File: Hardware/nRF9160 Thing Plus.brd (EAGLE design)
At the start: 58.4 x 22.9 mm, 128 parts, among them J1 USB Female C, J10 QWIIC_RIGHT_ANGLE, J2 CON-HEADER-1X12-MALE-PIN, J3 CON-HEADER-1X16-MALE-PIN, J4 CON-1909763-1, J6 CON-SIM-104224-0820, J7 CON-1909763-1, J8 CON-FTSH-105-XX-X-DV, Q1 MOSFET-P-SC89, Q2 MOSFET-DUAL-COMP-SOT563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

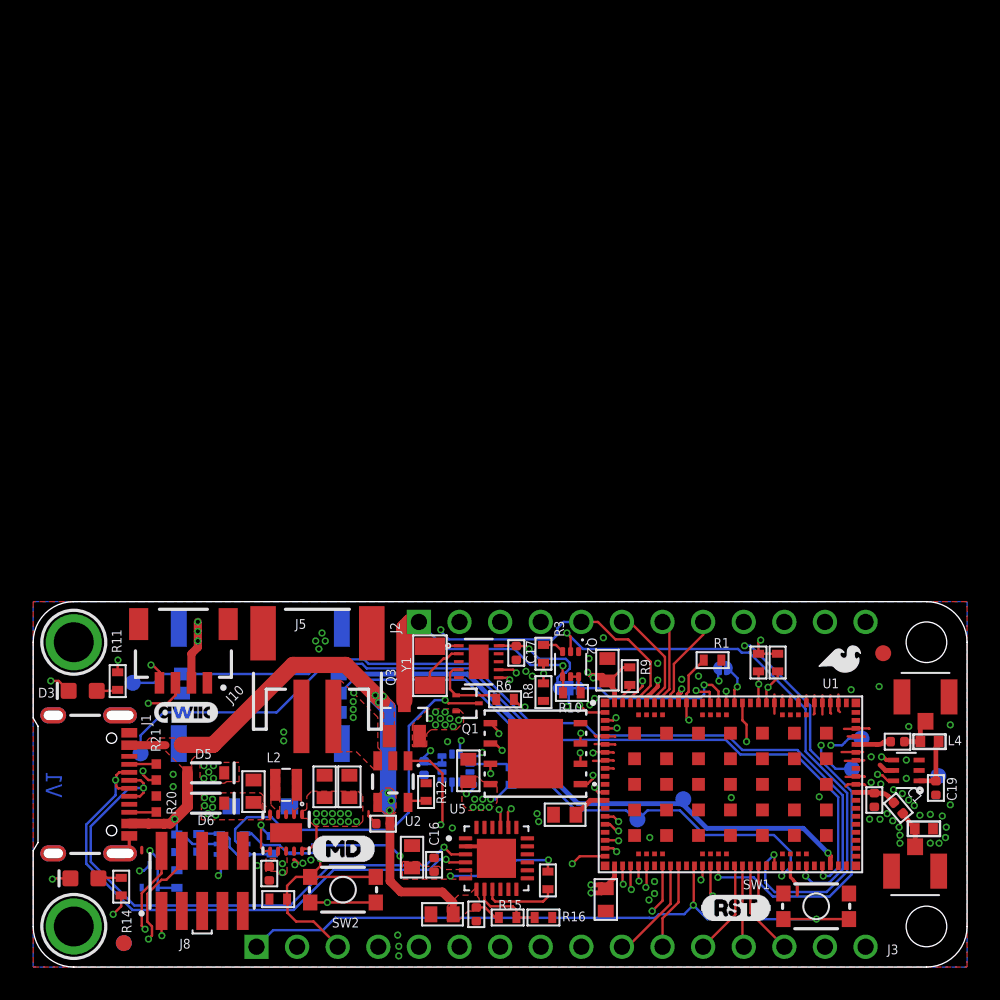
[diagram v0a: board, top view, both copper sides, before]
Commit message: Panel Fix
Issues spotted:
- USB-C connector was a two layer part instead of four. This caused an issue where the inner 3.3V copper layer was shorting to the ground layers on other layers through the USB support tabs.
- Running the panelizer tool cause Eagle to crash.

Changes Made:
- Replaced USB-C connector with 4-layer footprint varient
- Not sure what was causing Eagle to crash, but rotating the board 90 degrees fixed it
- Silk on the bottom layer wasn't orientated correctly after rotating the board. Checking the "spin" box on the silk flipped the silk like it should be for "Designed by", "X", "Y", and "Z" labels

Updated panel and gerbers with changes outlined above.
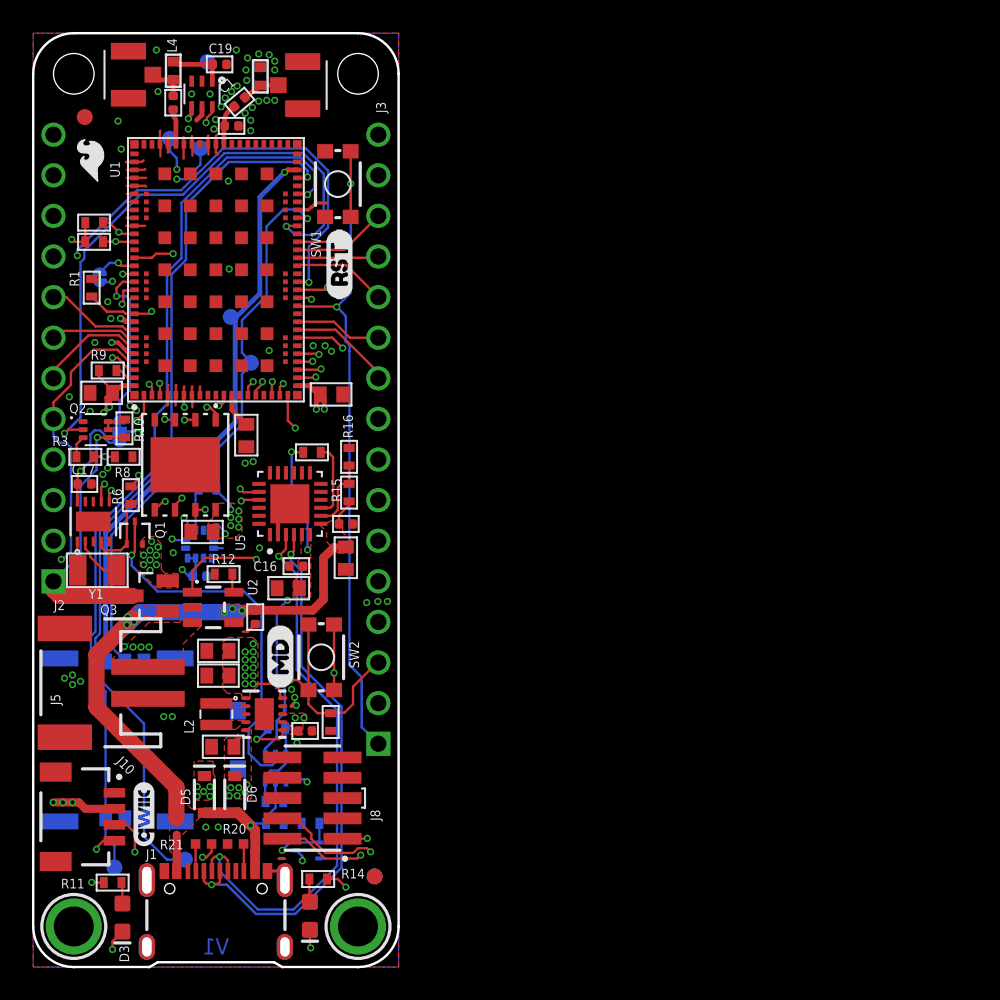
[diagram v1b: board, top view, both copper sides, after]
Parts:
- J1: device SparkFun-Connectors:USB-C-16P-2LAYER-PADS -> SparkFun-Connectors:USB-C-16P_4LAYER-PADS
- moved U$22 65.9 mm to (17.1, 57.7), turned to 270 degrees
- moved U$21 65.7 mm to (6.56, 57.6), turned to 270 degrees
- moved U$3 63.9 mm to (10.9, 56.6), turned to 270 degrees
- moved C19 63.7 mm to (11.7, 56.5), turned to 0 degrees
- moved J7 63.3 mm to (5.96, 55.8), turned to 90 degrees
- moved L4 63.2 mm to (8.76, 56.1), turned to 270 degrees
- moved L1 62.8 mm to (14.2, 55.7), turned to 270 degrees
- moved J4 62.3 mm to (16.9, 55.2), turned to 270 degrees
- moved U4 61.1 mm to (10.6, 54.6), turned to 180 degrees
- moved C12 60.4 mm to (8.76, 54.1), turned to 90 degrees
- moved C1 60.4 mm to (12.9, 54.1), turned to 220 degrees
- moved U$35 60.2 mm to (3.23, 53.2), turned to 0 degrees
- moved U$8 59.1 mm to (21.3, 52.1), turned to 0 degrees
- moved C2 58.3 mm to (12.4, 52.6), turned to 0 degrees
- moved U$13 57.7 mm to (7.82, 52.1), turned to 0 degrees
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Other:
- board size 58.4 x 22.9 mm -> 22.9 x 58.4 mm
- board text added: "Notes: * T4 solder paste * Lead Free assembly * Measures in inches"
- board text removed: "Notes: * T4 solder paste * Lead Free assembly * Measures in mm"
